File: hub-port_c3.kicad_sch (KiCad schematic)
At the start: 24 parts, among them J5 USB-C USB2.0, Q5 2N7002, U14 TPS2553DBVR, U18 USBLC6-2SC6, U20 TUSB320LAIRWBR, U35 SN74LVC1G04DBVR, U37 SN74LVC1G08DBVR, U39 SN74LVC1G04DBVR

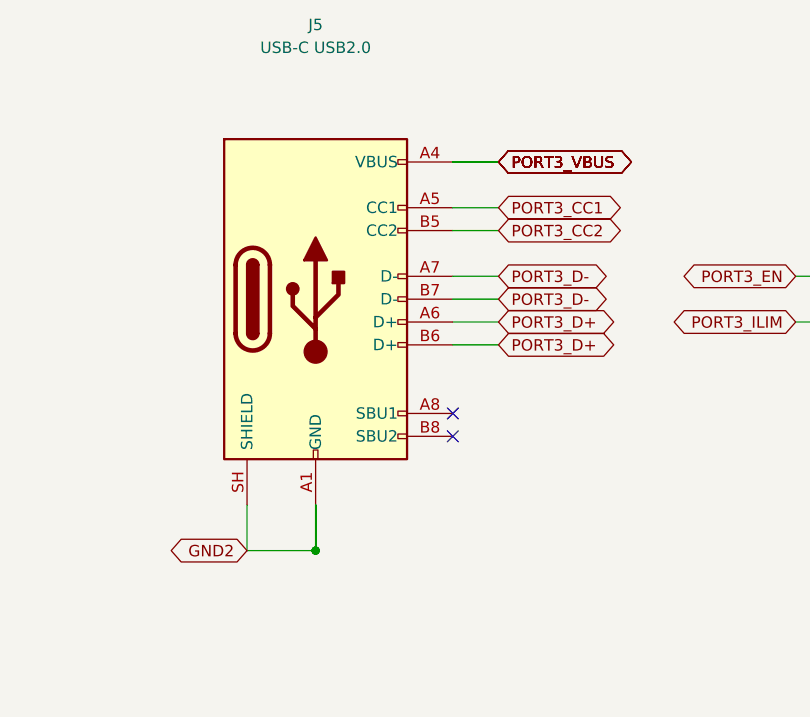
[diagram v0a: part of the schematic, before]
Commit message: feat(revc): assign exact BOM and verified local land patterns
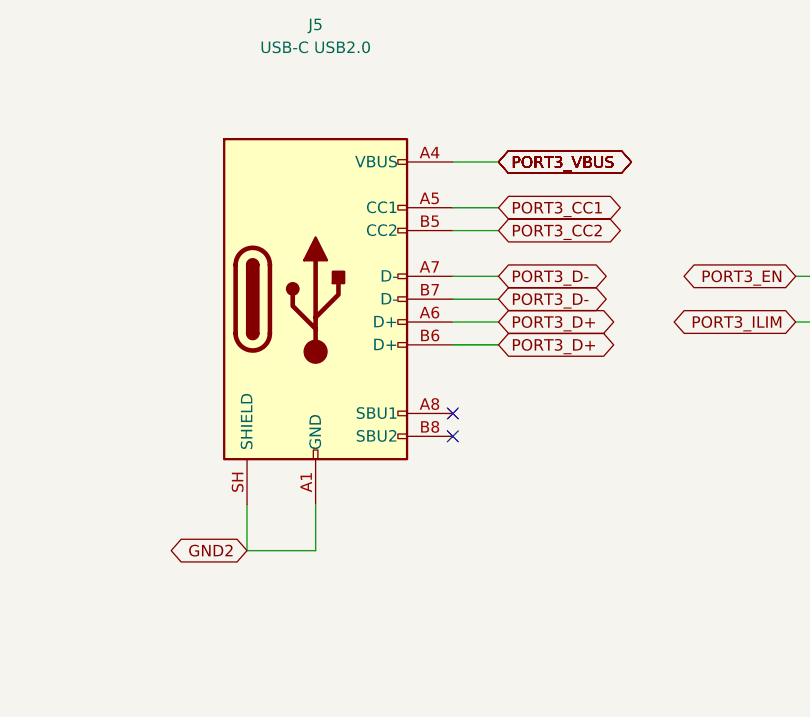
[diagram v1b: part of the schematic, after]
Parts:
- C100, C101, C102, C49, C51, C99: footprint (none) -> hub-lib:C_0402_1005Metric; LCSC (none) -> C77020; MPN (none) -> GRM155R71H104KE14D; Manufacturer (none) -> Murata Manufacturing; Ratings (none) -> 50V X7R 10%
- C50: footprint (none) -> hub-lib:C_0805_2012Metric; LCSC (none) -> C84416; MPN (none) -> GRM21BR61E106KA73L; Manufacturer (none) -> Murata Manufacturing; Ratings (none) -> 25V X5R 10%
- D10: footprint Diode_SMD:D_SOD-523 -> hub-lib:D_SOD-523; LCSC (none) -> C19950551; Ratings (none) -> See exact manufacturer datasheet
- J5: footprint Connector_USB:USB_C_Receptacle_HRO_TYPE-C-31-M-12 -> hub-lib:USB_C_Receptacle_HRO_TYPE-C-31-M-12; LCSC (none) -> C165948; Ratings (none) -> See exact manufacturer datasheet
- Q5: footprint Package_TO_SOT_SMD:SOT-23 -> hub-lib:SOT-23; LCSC (none) -> C65189; Ratings (none) -> See exact manufacturer datasheet
- R103, R49: footprint (none) -> hub-lib:R_0402_1005Metric; LCSC (none) -> C192169; MPN (none) -> ERJ2RKF1003X; Manufacturer (none) -> Panasonic Industry; Ratings (none) -> 1%, 0.1W, 50V
- R119, R73: footprint (none) -> hub-lib:R_0402_1005Metric; LCSC (none) -> C191123; MPN (none) -> ERJ2RKF1002X; Manufacturer (none) -> Panasonic Industry; Ratings (none) -> 1%, 0.1W, 50V
- R40: footprint (none) -> hub-lib:R_0402_1005Metric; LCSC (none) -> C416544; MPN (none) -> ERJ2RKF4642X; Manufacturer (none) -> Panasonic Industry; Ratings (none) -> 1%, 0.1W, 50V
- R72: footprint (none) -> hub-lib:R_0402_1005Metric; LCSC (none) -> C400631; MPN (none) -> ERJ2RKF4701X; Manufacturer (none) -> Panasonic Industry; Ratings (none) -> 1%, 0.1W, 50V
- R74: footprint (none) -> hub-lib:R_0402_1005Metric; LCSC (none) -> C2085054; MPN (none) -> ERJ2RKF9093X; Manufacturer (none) -> Panasonic Industry; Ratings (none) -> 1%, 0.1W, 50V
- R81: footprint (none) -> hub-lib:R_0805_2012Metric; LCSC (none) -> C193990; MPN (none) -> ERJ6ENF1000V; Manufacturer (none) -> Panasonic Industry; Ratings (none) -> 100R 1%, 0.125W; 0.14mJ maximum discharge pulse
- U14: footprint (none) -> hub-lib:SOT-23-6; LCSC (none) -> C55266; Ratings (none) -> See exact manufacturer datasheet
- U18: footprint Package_TO_SOT_SMD:SOT-23-6 -> hub-lib:SOT-23-6; LCSC (none) -> C7519; Ratings (none) -> See exact manufacturer datasheet
- U20: footprint (none) -> hub-lib:Texas_X2QFN-12_1.6x1.6mm_P0.4mm; LCSC (none) -> C132554; Ratings (none) -> See exact manufacturer datasheet
- U35, U39: footprint (none) -> hub-lib:SOT-23-5; LCSC (none) -> C7827; Ratings (none) -> See exact manufacturer datasheet
- U37: footprint (none) -> hub-lib:SOT-23-5; LCSC (none) -> C7666; Ratings (none) -> See exact manufacturer datasheet

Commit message: feat(revc): place synchronized unrouted board and correct bus startup
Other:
- note added: "Attach detection: DFP, default Rp, no VCONN"
- note added: "Attachment AND hub permission controls VBUS"
- note added: "Detach discharge, including total board power loss"
- note added: "Port 3: USB-C, USB 2.0 and ESD"
- note added: "USB 2.0 / 480 Mbps | Rev C electrical design | Placement and routing review pending"
- note removed: "Rev C | all routing reserved for Alex | electrical draft under review"
- moved on the sheet: C100, C101, C102, C49, C50, C51, C99, D10, J5, Q5, R103, R119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

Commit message: feat(revc): finish verified TI hub routing handoff
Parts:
- R81: Ratings 100R 1%, 0.125W; 0.14mJ maximum discharge pulse -> 100R 1%, 0.125W; 0.20mJ maximum design discharge pulse
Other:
- note added: "USB 2.0 / 480 Mbps | Rev C electrical design | Placed PCB; all routing by Alex; hardware tests pending"
- note removed: "USB 2.0 / 480 Mbps | Rev C electrical design | Placement and routing review pending"
- moved on the sheet: D10, Q5, R119, R81
